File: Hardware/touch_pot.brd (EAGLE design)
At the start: 44.5 x 78.7 mm, 79 parts, among them U1 PIC16F1829, U2 AD5262, U3 5V

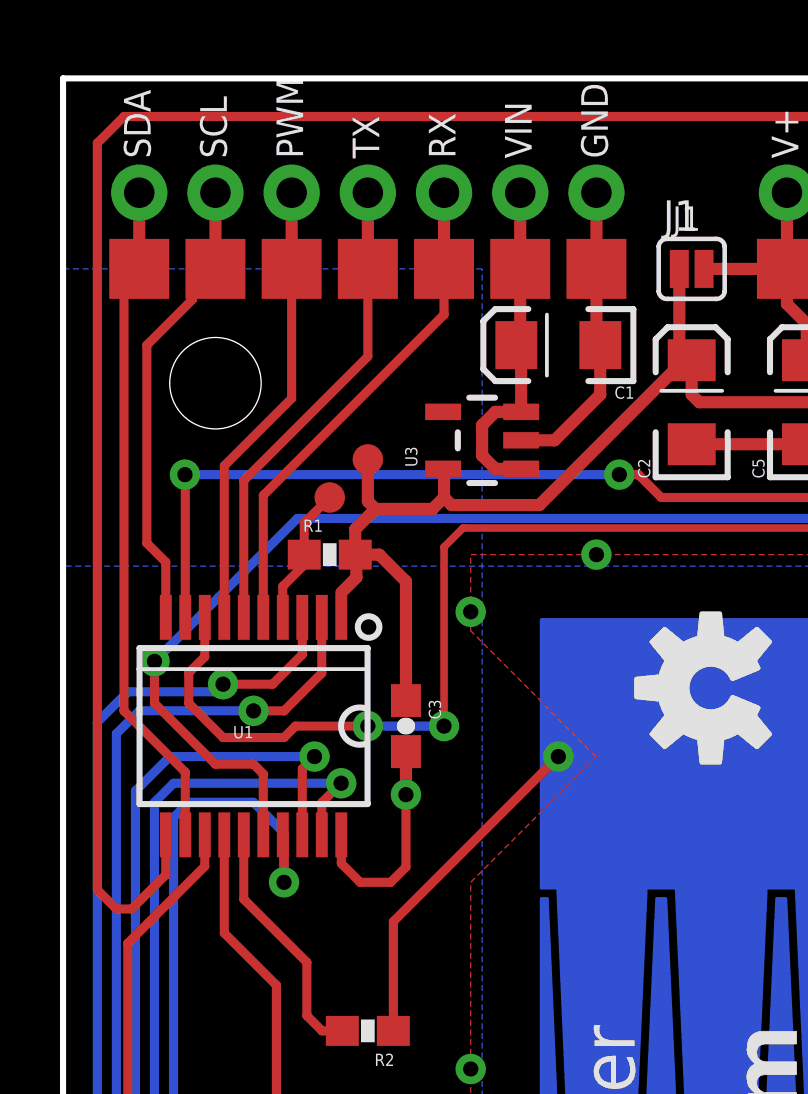
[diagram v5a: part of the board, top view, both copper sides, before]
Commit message: Changed pinout to standard I2C pinout
Changed pinout to standard I2C pinout
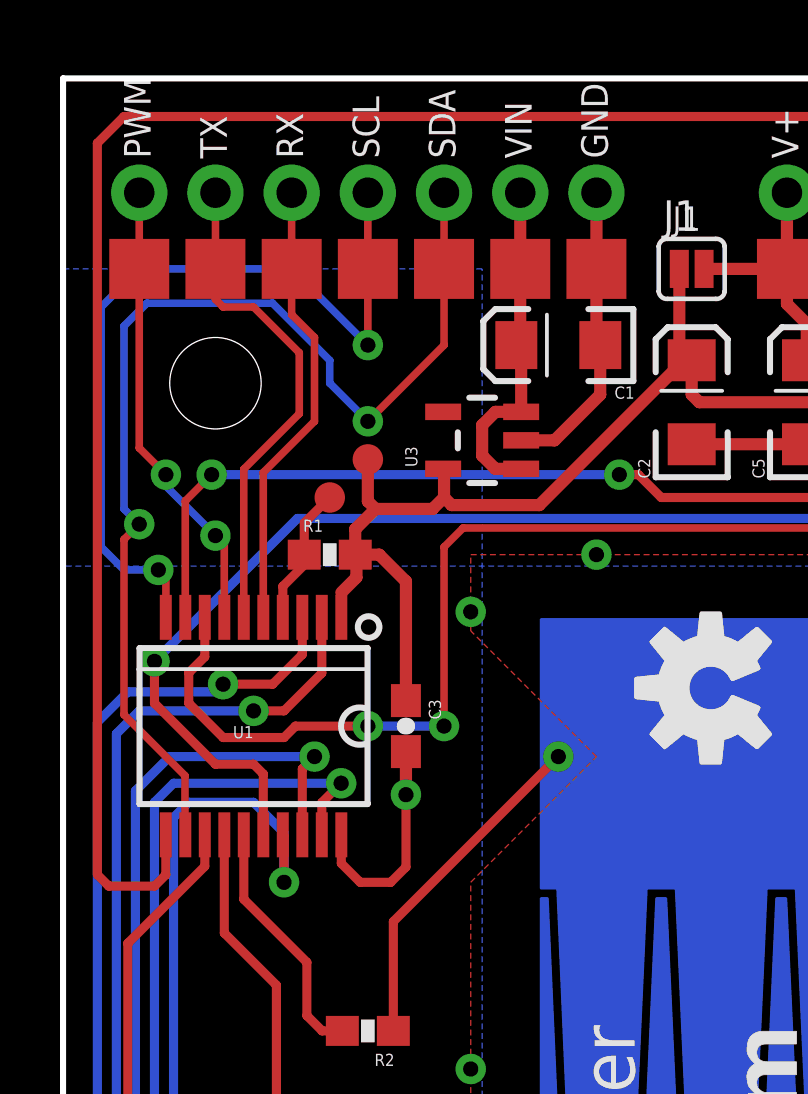
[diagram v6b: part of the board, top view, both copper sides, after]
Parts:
- moved CON1 10.2 mm to (12.7, 72.4)
- moved JP1 10.2 mm to (12.7, 74.9)
- moved CON2 5.08 mm to (10.2, 72.4)
- moved CON3 5.08 mm to (2.54, 72.4)
- moved CON5 5.08 mm to (5.08, 72.4)
- moved JP2 5.08 mm to (10.2, 74.9)
- moved JP3 5.08 mm to (2.54, 74.9)
- moved JP5 5.08 mm to (5.08, 74.9)
- moved CON4 5.08 mm to (7.62, 72.4)
- moved JP4 5.08 mm to (7.62, 74.9)
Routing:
- net SDA: track 22.5 -> 37.4 mm, vias 0 -> 2
- net SCL: track 15.4 -> 27.5 mm, vias 0 -> 2
- net RX: track 16.7 -> 15.2 mm
- net SCLK: track 97.0 -> 96.1 mm
- net TX: track 15.9 -> 16.7 mm
- net SDO: track 38.4 -> 37.8 mm
- net PWM_OUT: track 15.1 -> 15.3 mm, vias 0 -> 2

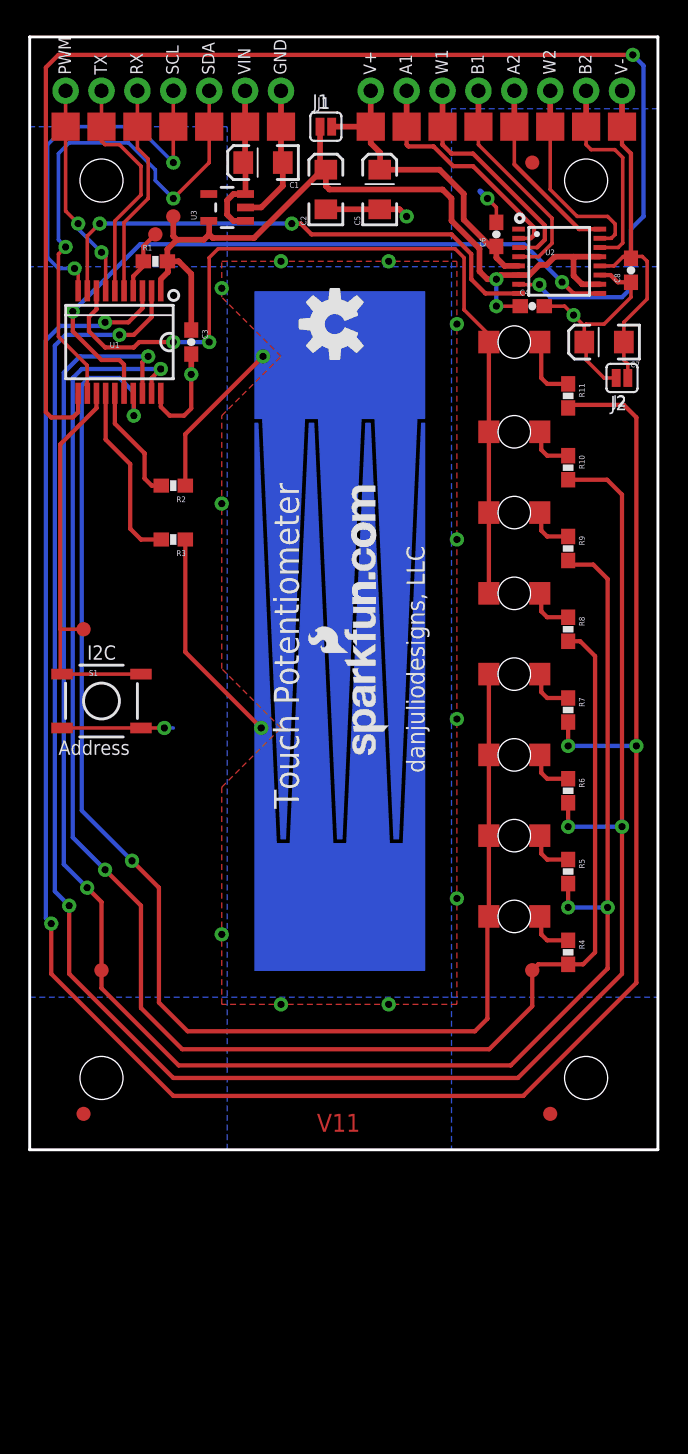
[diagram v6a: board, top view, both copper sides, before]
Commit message: Ready for Reds
Added note about Non-plated Thru Holes on the bottom-mounted LEDs,
added note about I2C addressing, added note about maximum and min.
voltages on V+ and V-, moved  VPP test point ever so slightly, added
polarity silk to bottom-mounted LEDs, added note in Sparkle about BLACK
SOLDERMASK.
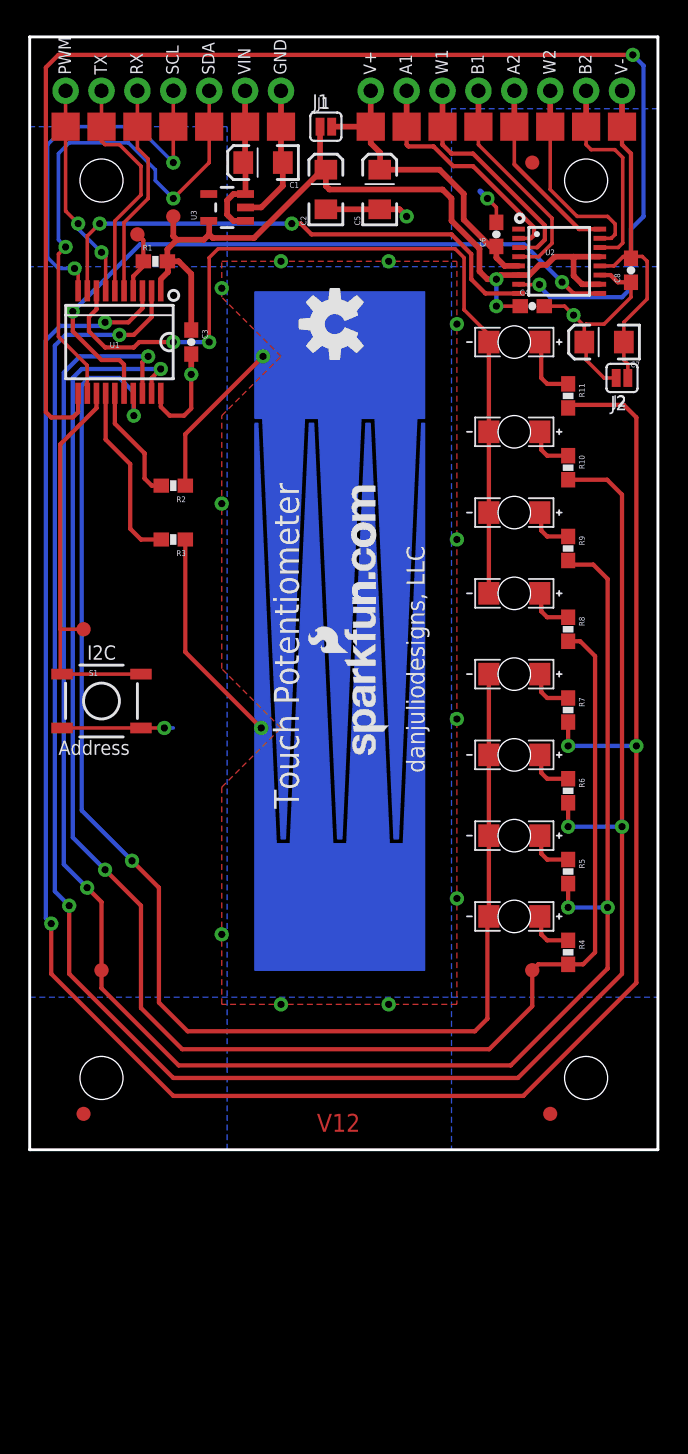
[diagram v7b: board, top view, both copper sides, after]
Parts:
- moved TP1 1.27 mm to (7.62, 64.8)
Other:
- board text added: "The 0.09055118 in. (2.3mm) hole is NPTH hole"
- board text added: "V12"
- board text removed: "V11"
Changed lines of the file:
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@@
 <?xml version="1.0" encoding="utf-8"?>
 <!DOCTYPE eagle SYSTEM "eagle.dtd">
-<eagle version="7.1.0">
+<eagle version="7.2.0">
 <drawing>
 <settings>
@@
 <text x="42.291" y="76.073" size="0.889" layer="21" ratio="15" rot="R90">V-</text>
 <text x="53.34" y="-16.51" size="1.778" layer="51" font="vector" ratio="10">danjuliodesigns, LLC</text>
-<text x="20.32" y="1.27" size="1.27" layer="1" font="vector" ratio="15" distance="45">V11</text>
+<text x="20.32" y="1.27" size="1.27" layer="1" font="vector" ratio="15" distance="45">V12</text>
 <text x="4.064" y="34.671" size="1.016" layer="21" font="vector" ratio="15">I2C</text>
 <text x="2.032" y="27.94" size="1.016" layer="21" font="vector" ratio="15">Address</text>
@@
 <dimension x1="5.08" y1="68.58" x2="0" y2="68.58" x3="2.54" y3="80.01" textsize="1.778" textratio="15" layer="51" unit="inch"/>
 <dimension x1="5.08" y1="5.08" x2="39.37" y2="5.08" x3="22.225" y3="83.82" textsize="1.778" textratio="15" layer="51" unit="inch"/>
+<text x="48.26" y="36.83" size="1.778" layer="51" font="vector" ratio="15">The 0.09055118 in. (2.3mm) hole is NPTH hole</text>
 </plain>
 <attributes>
@@
 <element name="TP2" library="SparkFun-Passives" package="PAD.03X.04" value="" x="10.16" y="66.04"/>
 <element name="TP3" library="SparkFun-Passives" package="PAD.03X.04" value="" x="3.81" y="36.83"/>
-<element name="TP1" library="SparkFun-Passives" package="PAD.03X.04" value="" x="8.89" y="64.77"/>
+<element name="TP1" library="SparkFun-Passives" package="PAD.03X.04" value="" x="7.62" y="64.77"/>
 <element name="TP4" library="SparkFun-Passives" package="PAD.03X.04" value="" x="35.56" y="12.7"/>
 <element name="TP5" library="SparkFun-Passives" package="PAD.03X.04" value="" x="5.08" y="12.7"/>
@@
 <contactref element="TP1" pad="P$1"/>
 <wire x1="8.04" y1="62.523" x2="7.325" y2="61.808" width="0.3048" layer="1"/>
-<wire x1="8.04" y1="63.92" x2="8.89" y2="64.77" width="0.3048" layer="1"/>
 <contactref element="R1" pad="1"/>
-<wire x1="8.04" y1="63.92" x2="8.04" y2="62.865" width="0.3048" layer="1"/>
+<wire x1="8.04" y1="64.35" x2="8.04" y2="62.865" width="0.3048" layer="1"/>
 <wire x1="8.04" y1="62.523" x2="8.04" y2="62.865" width="0.3048" layer="1"/>
 <contactref element="U1" pad="4"/>
 <wire x1="7.325" y1="60.775" x2="7.325" y2="61.808" width="0.3048" layer="1"/>
+<wire x1="8.04" y1="64.35" x2="7.62" y2="64.77" width="0.3048" layer="1"/>
 </signal>
 <signal name="SDA">

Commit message: replaced fids with SFE fids
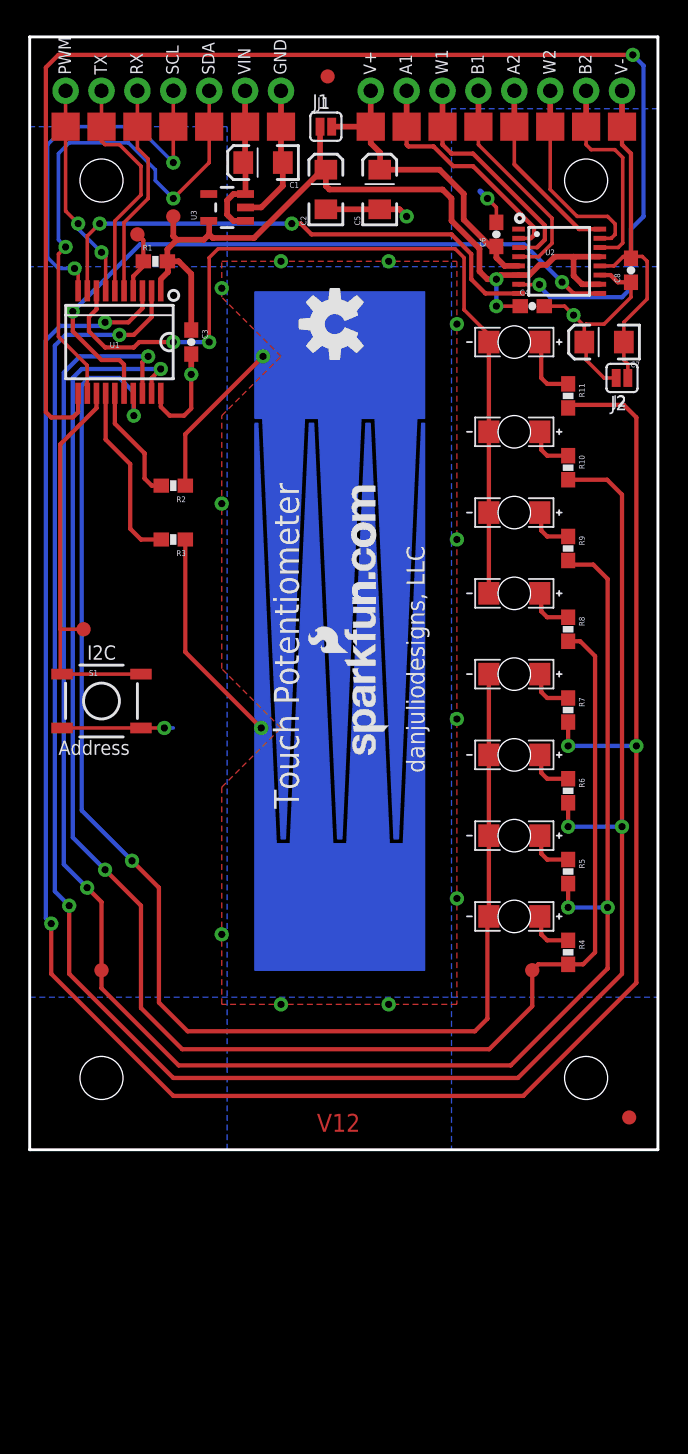
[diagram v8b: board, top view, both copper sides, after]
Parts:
- removed U$1, U$2, U$3: FIDUCIAL, djd_eagle_library:FIDUCIAL
- added FID1, FID2: FIDUCIAL1X2, SparkFun-Aesthetics:FIDUCIAL-1X2
